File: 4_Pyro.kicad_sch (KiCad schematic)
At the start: 37 parts, among them J501 XT60-M, Q501 IRLZ44N, Q502 IRLZ44N, Q503 IRLZ44N, Q504 IRLZ44N, Q505 IRLZ44N, Q506 IRLZ44N, U501 PC817, U502 PC817, U503 CD4051B, U504 PC817, U505 PC817, U506 PC817, U507 PC817

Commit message: Major changes
Updated schematic for better power delivery
Changed 3.3V supply to buck converter instead of LDO due to heat
Deleted the entire PCB, redoing the whole thing due to problems in
laying traces that made some connections impossible to make
Also updated README to reflect these changes
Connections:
- net PYRO_0: no longer R505.2, U503.15 (X2)
- net PYRO_1: no longer R506.2, U503.14 (X1)
- net PYRO_2: no longer R513.2, U503.13 (X0)
- net PYRO_3: no longer R514.2, U503.12 (X3)
- net PYRO_4: no longer R519.2, U503.1 (X4)
- net PYRO_5: no longer R520.2, U503.5 (X5)
- new net PYRO_C0: R505.2, U503.15 (X2)
- new net PYRO_C1: R506.2, U503.14 (X1)
- new net PYRO_C2: R513.2, U503.13 (X0)
- new net PYRO_C3: R514.2, U503.12 (X3)
- new net PYRO_C4: R519.2, U503.1 (X4)
- new net PYRO_C5: R520.2, U503.5 (X5)
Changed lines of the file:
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@@
 		)
 	)
-	(label "PYRO_4"
+	(label "PYRO_C4"
 		(at 44.45 153.67 0)
 		(effects
@@
 		)
 	)
-	(label "PYRO_2"
+	(label "PYRO_C2"
 		(at 44.45 143.51 0)
 		(effects
@@
 		)
 	)
-	(label "PYRO_5"
+	(label "PYRO_C5"
 		(at 44.45 156.21 0)
 		(effects
@@
 		)
 	)
-	(label "PYRO_5"
+	(label "PYRO_C5"
 		(at 236.22 96.52 180)
 		(effects
@@
 		)
 	)
-	(label "PYRO_1"
+	(label "PYRO_C1"
 		(at 44.45 146.05 0)
 		(effects
@@
 		)
 	)
-	(label "PYRO_3"
+	(label "PYRO_C3"
 		(at 44.45 151.13 0)
 		(effects
@@
 		)
 	)
-	(label "PYRO_0"
+	(label "PYRO_C0"
 		(at 44.45 148.59 0)
 		(effects
@@
 		)
 	)
-	(label "PYRO_4"
+	(label "PYRO_C4"
 		(at 236.22 57.15 180)
 		(effects
@@
 		)
 	)
-	(label "PYRO_2"
+	(label "PYRO_C2"
 		(at 171.45 57.15 180)
 		(effects
@@
 		)
 	)
-	(label "PYRO_3"
+	(label "PYRO_C3"
 		(at 171.45 96.52 180)
 		(effects
@@
 		)
 	)
-	(label "PYRO_0"
+	(label "PYRO_C0"
 		(at 104.14 58.42 180)
 		(effects
@@
 		)
 	)
-	(label "PYRO_1"
+	(label "PYRO_C1"
 		(at 104.14 97.79 180)
 		(effects

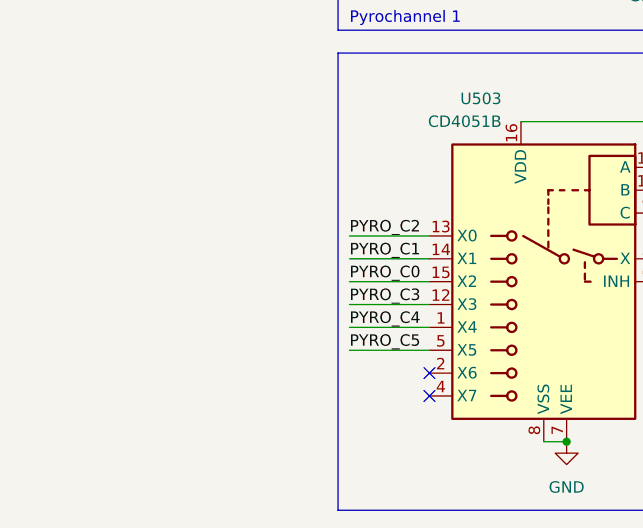
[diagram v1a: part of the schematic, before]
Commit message: Added more power (3.3V) headers for more powering peripherals
Continued laying out tracks
Revised order of connections to pyrochannel mux for easier routing
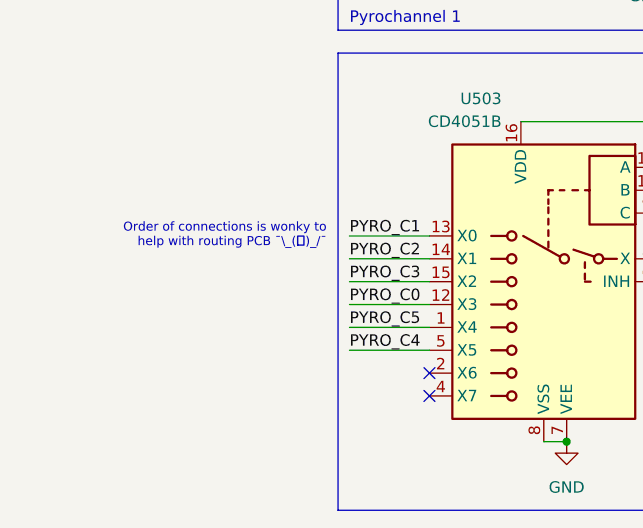
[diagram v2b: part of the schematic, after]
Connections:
- net PYRO_C0: now also U503.12 (X3); no longer U503.15 (X2)
- net PYRO_C1: now also U503.13 (X0); no longer U503.14 (X1)
- net PYRO_C2: now also U503.14 (X1); no longer U503.13 (X0)
- net PYRO_C3: now also U503.15 (X2); no longer U503.12 (X3)
- net PYRO_C4: now also U503.5 (X5); no longer U503.1 (X4)
- net PYRO_C5: now also U503.1 (X4); no longer U503.5 (X5)
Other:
- note added: "Order of connections is wonky to help with routing PCB ¯\_(ツ)_/¯"
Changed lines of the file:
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@@
+		)
+	)
+	(text "Order of connections is wonky to \nhelp with routing PCB ¯\\_(ツ)_/¯"
+		(exclude_from_sim no)
+		(at 41.91 143.51 0)
+		(effects
+			(font
+				(face "KiCad Font")
+				(size 1 1)
+			)
+			(justify right)
 		)
 	)
@@
 		)
 	)
+	(label "PYRO_C5"
+		(at 44.45 153.67 0)
+		(effects
+			(font
+				(size 1.27 1.27)
+			)
+			(justify left bottom)
+		)
+	)
+	(label "PYRO_C1"
+		(at 44.45 143.51 0)
+		(effects
+			(font
+				(size 1.27 1.27)
+			)
+			(justify left bottom)
+		)
+	)
 	(label "PYRO_C4"
-		(at 44.45 153.67 0)
-		(effects
-			(font
-				(size 1.27 1.27)
-			)
-			(justify left bottom)
-		)
-	)
-	(label "PYRO_C2"
-		(at 44.45 143.51 0)
-		(effects
-			(font
-				(size 1.27 1.27)
-			)
-			(justify left bottom)
-		)
-	)
-	(label "PYRO_C5"
 		(at 44.45 156.21 0)
 		(effects
@@
 		)
 	)
-	(label "PYRO_C1"
+	(label "PYRO_C2"
 		(at 44.45 146.05 0)
 		(effects
@@
 		)
 	)
+	(label "PYRO_C0"
+		(at 44.45 151.13 0)
+		(effects
+			(font
+				(size 1.27 1.27)
+			)
+			(justify left bottom)
+		)
+	)
 	(label "PYRO_C3"
-		(at 44.45 151.13 0)
-		(effects
-			(font
-				(size 1.27 1.27)
-			)
-			(justify left bottom)
-		)
-	)
-	(label "PYRO_C0"
 		(at 44.45 148.59 0)
 		(effects
